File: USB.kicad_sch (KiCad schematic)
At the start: 34 parts, among them J1 USB_C_Receptable_USB2.0, U1 AP2141WG-7, U2 3V3

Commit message: Apply suggestions from Petr Dvorak
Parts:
- added C42: 100n, Capacitor_SMD:C_0402_1005Metric_Pad0.74x0.62mm_HandSolder, symbol Device:C
- added C43: 10u, Capacitor_SMD:C_0805_2012Metric, symbol Device:C
- C1, C2: Comment 50V 100nF X7R ±10% 0402 Multilayer Ceramic Capacitors MLCC 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 -> 50V 100nF X7R ±10% 0402
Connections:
- net GND: now also C42.1, C43.2
- net at D1.1 (A1), F1.2, U1.5 (IN): now also C42.2, C43.1
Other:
- moved on the sheet: C1, C10, C11, C12, C13, C14, C15, C16, C17, C2, D1, D2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

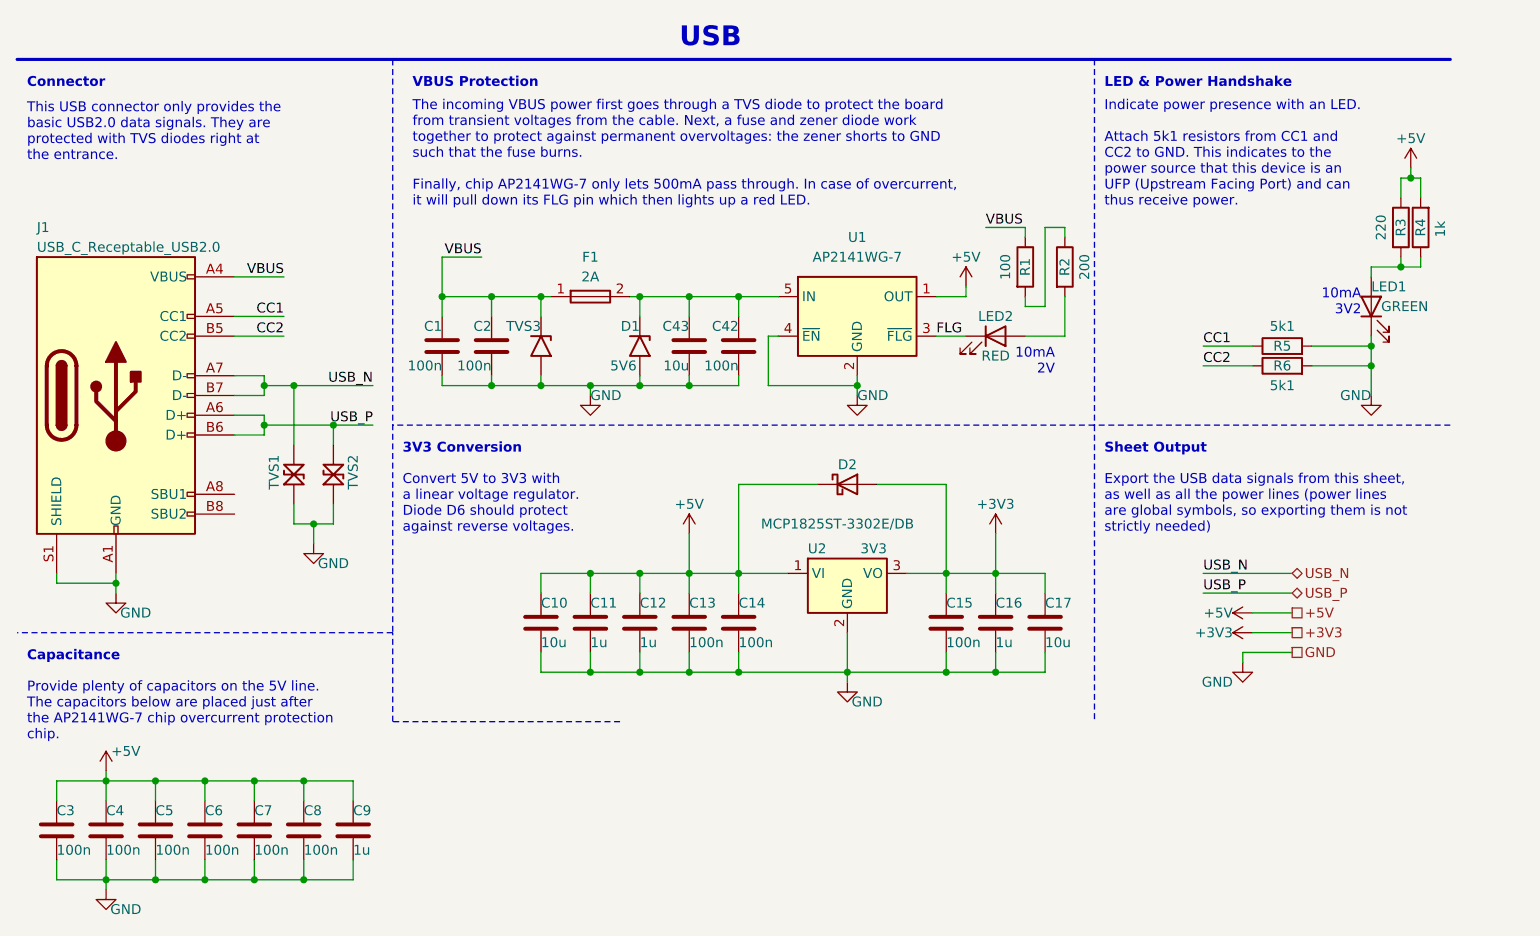
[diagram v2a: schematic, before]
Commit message: Rename capacitors
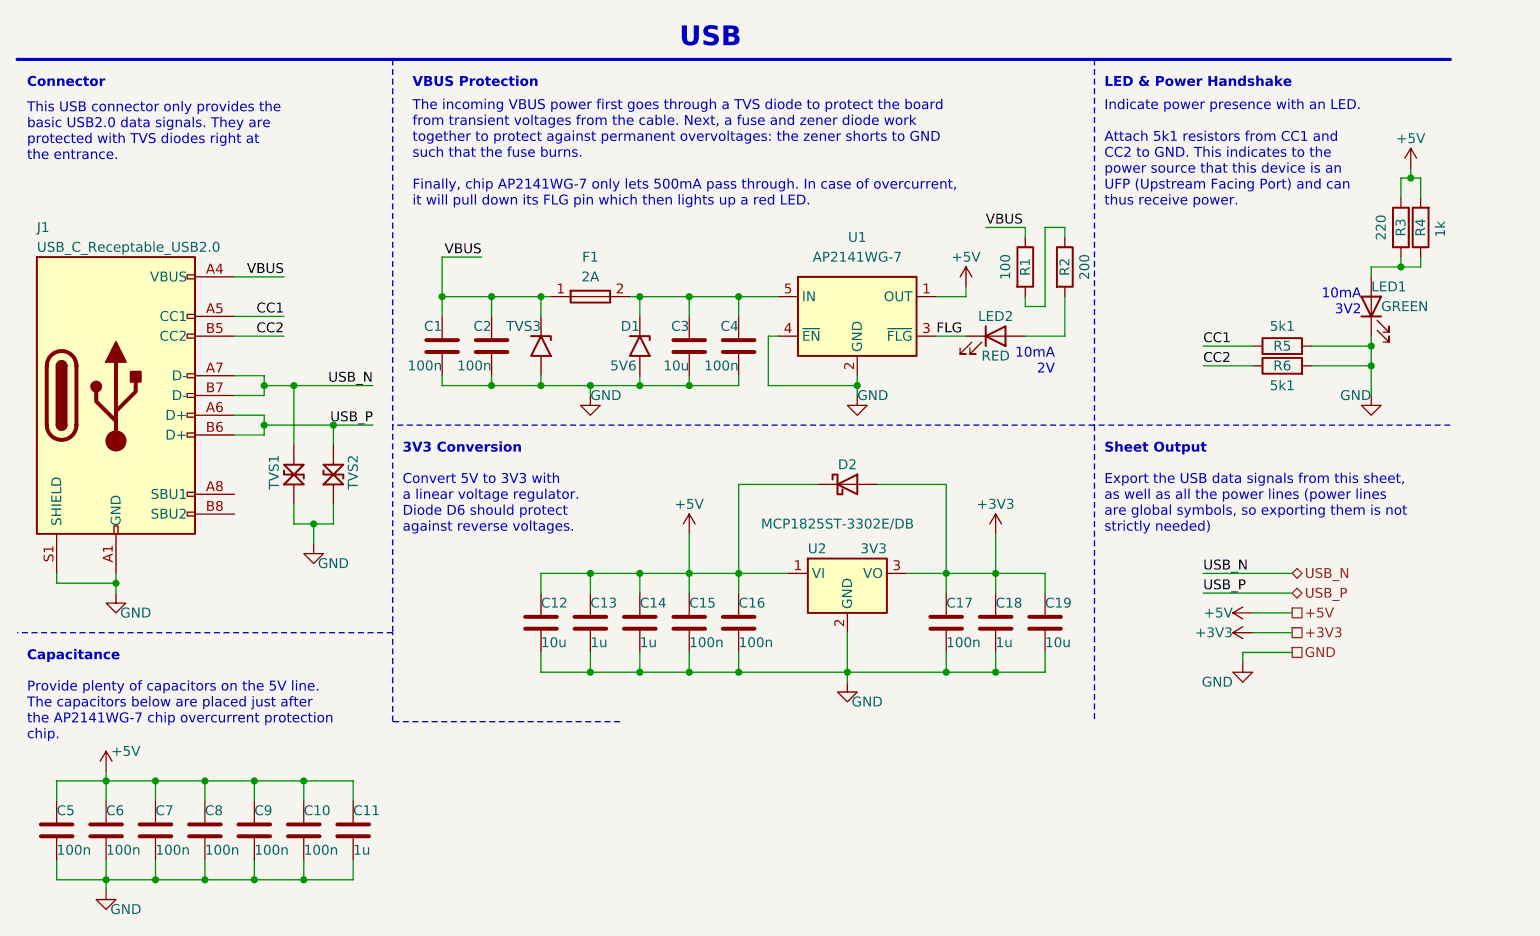
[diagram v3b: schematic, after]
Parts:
- C10: renamed from C8; Comment (none) -> 16V 100nF X7R ±10% 0402
- C11: renamed from C9; Comment (none) -> 25V 1uF X5R ±10% 0402
- C12: renamed from C10; Comment (none) -> 6.3V 10uF X5R ±20% 0402
- C13: renamed from C11; Comment (none) -> 25V 1uF X5R ±10% 0402
- C14: renamed from C12; Comment (none) -> 25V 1uF X5R ±10% 0402
- C15: renamed from C13; Comment (none) -> 16V 100nF X7R ±10% 0402
- C16: renamed from C14; Comment (none) -> 16V 100nF X7R ±10% 0402
- C17: renamed from C15; Comment (none) -> 16V 100nF X7R ±10% 0402
- C18: renamed from C16; Comment (none) -> 25V 1uF X5R ±10% 0402
- C19: renamed from C17; Comment (none) -> 6.3V 10uF X5R ±20% 0402
- C5: renamed from C3; Comment (none) -> 16V 100nF X7R ±10% 0402
- C6: renamed from C4; Comment (none) -> 16V 100nF X7R ±10% 0402
- C7: renamed from C5; Comment (none) -> 16V 100nF X7R ±10% 0402
- C8: renamed from C6; Comment (none) -> 16V 100nF X7R ±10% 0402
- C9: renamed from C7; Comment (none) -> 16V 100nF X7R ±10% 0402
- renumbered C43 to C3, C42 to C4

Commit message: Add production files
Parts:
- TVS3: SPN SMAJ5.0ALFTR-ND -> (none); Supplier DigiKey -> (none)
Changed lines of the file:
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@@
-      (effects (font (size 1.27 1.27)) hide)
-    )
-    (property "Supplier" "DigiKey" (at 87.63 55.88 0)
-      (effects (font (size 1.27 1.27)) hide)
-    )
-    (property "SPN" "SMAJ5.0ALFTR-ND" (at 90.17 55.88 0)
       (effects (font (size 1.27 1.27)) hide)
     )

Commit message: Work on BOM
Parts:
- LED1: JLCPCB Part # (none) -> C7115899
- LED2: JLCPCB Part # (none) -> C5579175
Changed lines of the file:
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@@
       (effects (font (size 1.27 1.27)) hide)
     )
-    (property "JLCPCB Part #" "" (at 173.99 50.8 0)
+    (property "JLCPCB Part #" "C7115899" (at 173.99 50.8 0)
       (effects (font (size 1.27 1.27)) hide)
     )
@@
       (effects (font (size 1.27 1.27)) hide)
     )
-    (property "JLCPCB Part #" "" (at 138.43 41.91 0)
-      (effects (font (size 1.27 1.27)) hide)
-    )
+    (property "JLCPCB Part #" "C5579175" (at 138.43 41.91 0)
+      (effects (font (size 1.27 1.27)) hide)
+    )

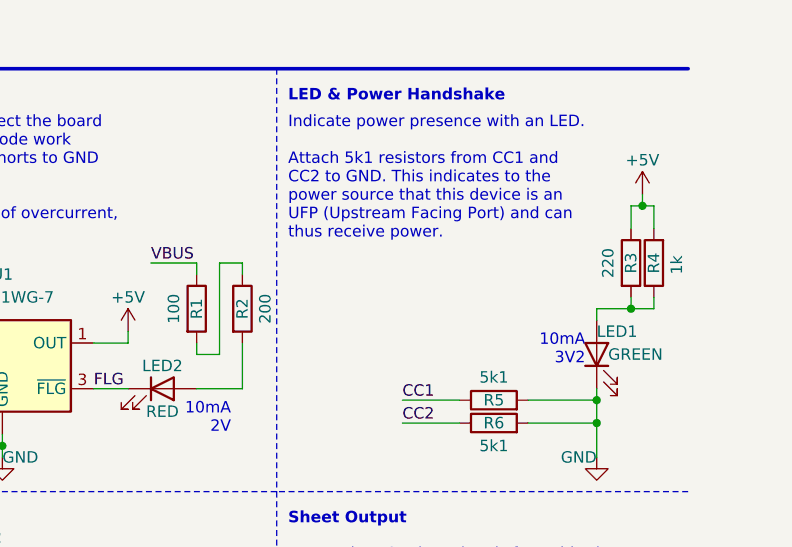
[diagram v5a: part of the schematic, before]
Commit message: Modify resistors for LEDs
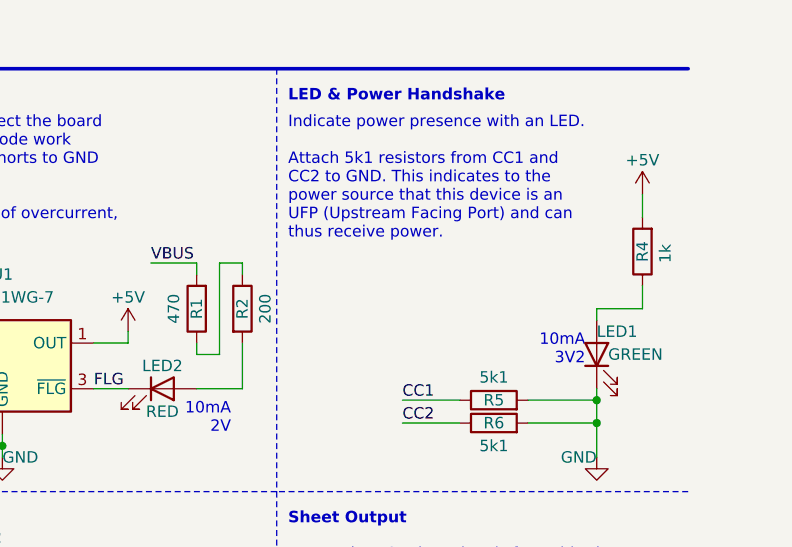
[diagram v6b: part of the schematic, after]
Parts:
- removed R3: 220, Resistor_SMD:R_0402_1005Metric_Pad0.72x0.64mm_HandSolder, symbol Device:R
- R1: value 100 -> 470; JLCPCB Part # C25076 -> C25117; MPN 0402WGF1000TCE -> 0402WGF4700TCE
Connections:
- net VBUS: now also R1.2; no longer R1.1
- net at R2.1: now also R1.1; no longer R1.2
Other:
- moved on the sheet: R4
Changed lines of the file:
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@@
   (junction (at 92.71 49.53) (diameter 0) (color 0 0 0 0)
   )
-  (junction (at 190.5 45.72) (diameter 0) (color 0 0 0 0)
-  )
   (junction (at 36.83 111.76) (diameter 0) (color 0 0 0 0)
   )
@@
   (junction (at 67.31 49.53) (diameter 0) (color 0 0 0 0)
   )
-  (junction (at 191.77 34.29) (diameter 0) (color 0 0 0 0)
-  )
   (junction (at 105.41 97.79) (diameter 0) (color 0 0 0 0)
   )
@@
   )
   (wire (pts (xy 86.36 97.79) (xy 92.71 97.79))
-    (stroke (width 0) (type default))
-  )
-  (wire (pts (xy 193.04 34.29) (xy 191.77 34.29))
     (stroke (width 0) (type default))
   )
@@
     (stroke (width 0) (type default))
   )
-  (wire (pts (xy 193.04 36.83) (xy 193.04 34.29))
+  (wire (pts (xy 191.77 33.02) (xy 191.77 35.56))
     (stroke (width 0) (type default))
   )
@@
     (stroke (width 0) (type default))
   )
-  (wire (pts (xy 193.04 44.45) (xy 193.04 45.72))
+  (wire (pts (xy 191.77 43.18) (xy 191.77 45.72))
     (stroke (width 0) (type default))
   )
@@
   )
   (wire (pts (xy 80.01 97.79) (xy 86.36 97.79))
-    (stroke (width 0) (type default))
-  )
-  (wire (pts (xy 190.5 45.72) (xy 193.04 45.72))
     (stroke (width 0) (type default))
   )
@@
     (stroke (width 0) (type default))
   )
-  (wire (pts (xy 186.69 45.72) (xy 190.5 45.72))
+  (wire (pts (xy 186.69 45.72) (xy 191.77 45.72))
     (stroke (width 0) (type default))
   )
@@
   )
   (wire (pts (xy 24.13 124.46) (xy 24.13 125.73))
-    (stroke (width 0) (type default))
-  )
-  (wire (pts (xy 190.5 44.45) (xy 190.5 45.72))
     (stroke (width 0) (type default))
   )
@@
     (stroke (width 0) (type default))
   )
-  (wire (pts (xy 190.5 34.29) (xy 190.5 36.83))
-    (stroke (width 0) (type default))
-  )
   (wire (pts (xy 67.31 44.45) (xy 67.31 49.53))
     (stroke (width 0) (type default))
@@
     (stroke (width 0) (type dash))
   )
-  (wire (pts (xy 190.5 34.29) (xy 191.77 34.29))
-    (stroke (width 0) (type default))
-  )
   (wire (pts (xy 44.45 59.69) (xy 44.45 60.96))
     (stroke (width 0) (type default))
@@
   )
   (wire (pts (xy 99.06 80.01) (xy 99.06 85.09))
-    (stroke (width 0) (type default))
-  )
-  (wire (pts (xy 191.77 34.29) (xy 191.77 33.02))
     (stroke (width 0) (type default))
   )
@@
     )
   )
-  (symbol (lib_id "Device:R") (at 193.04 40.64 180) (unit 1)
-    (in_bom yes) (on_board yes) (dnp no)
-    (property "Reference" "R4" (at 193.04 40.64 90)
+  (symbol (lib_id "Device:R") (at 191.77 39.37 180) (unit 1)
+    (in_bom yes) (on_board yes) (dnp no)
+    (property "Reference" "R4" (at 191.77 39.37 90)
       (effects (font (size 1.27 1.27)))
     )
-    (property "Value" "1k" (at 195.58 41.91 90)
+    (property "Value" "1k" (at 194.31 40.64 90)
       (effects (font (size 1.27 1.27)) (justify right))
     )
-    (property "Footprint" "Resistor_SMD:R_0402_1005Metric_Pad0.72x0.64mm_HandSolder" (at 194.818 40.64 90)
-      (effects (font (size 1.27 1.27)) hide)
-    )
-    (property "Datasheet" "~" (at 193.04 40.64 0)
-      (effects (font (size 1.27 1.27)) hide)
-    )
-    (property "Manufacturer" "UNI-ROYAL(Uniroyal Elec)" (at 193.04 40.64 0)
-      (effects (font (size 1.27 1.27)) hide)
-    )
-    (property "MPN" "0402WGF1001TCE" (at 193.04 40.64 90)
-      (effects (font (size 1.27 1.27)) hide)
-    )
-    (property "JLCPCB Part #" "C11702" (at 193.04 40.64 90)
+    (property "Footprint" "Resistor_SMD:R_0402_1005Metric_Pad0.72x0.64mm_HandSolder" (at 193.548 39.37 90)
+      (effects (font (size 1.27 1.27)) hide)
+    )
+    (property "Datasheet" "~" (at 191.77 39.37 0)
+      (effects (font (size 1.27 1.27)) hide)
+    )
+    (property "Manufacturer" "UNI-ROYAL(Uniroyal Elec)" (at 191.77 39.37 0)
+      (effects (font (size 1.27 1.27)) hide)
+    )
+    (property "MPN" "0402WGF1001TCE" (at 191.77 39.37 90)
+      (effects (font (size 1.27 1.27)) hide)
+    )
+    (property "JLCPCB Part #" "C11702" (at 191.77 39.37 90)
       (effects (font (size 1.27 1.27)) hide)
     )
@@
     )
   )
-  (symbol (lib_id "Device:R") (at 142.24 45.72 0) (unit 1)
+  (symbol (lib_id "Device:R") (at 142.24 45.72 180) (unit 1)
     (in_bom yes) (on_board yes) (dnp no)
     (property "Reference" "R1" (at 142.24 45.72 90)
       (effects (font (size 1.27 1.27)))
     )
-    (property "Value" "100" (at 139.7 45.72 90)
+    (property "Value" "470" (at 139.7 45.72 90)
       (effects (font (size 1.27 1.27)))
     )
-    (property "Footprint" "Resistor_SMD:R_0402_1005Metric_Pad0.72x0.64mm_HandSolder" (at 140.462 45.72 90)
+    (property "Footprint" "Resistor_SMD:R_0402_1005Metric_Pad0.72x0.64mm_HandSolder" (at 144.018 45.72 90)
       (effects (font (size 1.27 1.27)) hide)
     )
@@
       (effects (font (size 1.27 1.27)) hide)
     )
-    (property "Manufacturer" "UNI-ROYAL(Uniroyal Elec)" (at 142.24 45.72 90)
-      (effects (font (size 1.27 1.27)) hide)
-    )
-    (property "MPN" "0402WGF1000TCE" (at 142.24 45.72 90)
-      (effects (font (size 1.27 1.27)) hide)
-    )
-    (property "JLCPCB Part #" "C25076" (at 142.24 45.72 90)
+    (property "Manufacturer" "UNI-ROYAL(Uniroyal Elec)" (at 142.24 45.72 0)
+      (effects (font (size 1.27 1.27)) hide)
+    )
+    (property "MPN" "0402WGF4700TCE" (at 142.24 45.72 90)
+      (effects (font (size 1.27 1.27)) hide)
+    )
+    (property "JLCPCB Part #" "C25117" (at 142.24 45.72 90)
       (effects (font (size 1.27 1.27)) hide)
     )
@@
         )
       )
-    )
-  )
-  (symbol (lib_id "Device:R") (at 190.5 40.64 0) (unit 1)
-    (in_bom yes) (on_board yes) (dnp no)
-    (property "Reference" "R3" (at 190.5 40.64 90)
-      (effects (font (size 1.27 1.27)))
-    )
-    (property "Value" "220" (at 187.96 40.64 90)
-      (effects (font (size 1.27 1.27)))
-    )
-    (property "Footprint" "Resistor_SMD:R_0402_1005Metric_Pad0.72x0.64mm_HandSolder" (at 188.722 40.64 90)
-      (effects (font (size 1.27 1.27)) hide)
-    )
-    (property "Datasheet" "~" (at 190.5 40.64 0)
-      (effects (font (size 1.27 1.27)) hide)
-    )
-    (property "Manufacturer" "UNI-ROYAL(Uniroyal Elec)" (at 190.5 40.64 90)
-      (effects (font (size 1.27 1.27)) hide)
-    )
-    (property "MPN" "0402WGF2200TCE" (at 190.5 40.64 90)
-      (effects (font (size 1.27 1.27)) hide)
-    )
-    (property "JLCPCB Part #" "C25091" (at 190.5 40.64 90)
-      (effects (font (size 1.27 1.27)) hide)
-    )
-    (pin "2")
-    (pin "1")
-    (instances
-      (project "tiny-scarab"
-        (path "/156c5422-ee07-49a4-8263-a2dbd26b90bd/99c48f54-1f97-4ff9-8db4-28f0cf987802"
-          (reference "R3") (unit 1)
-        )
-      )

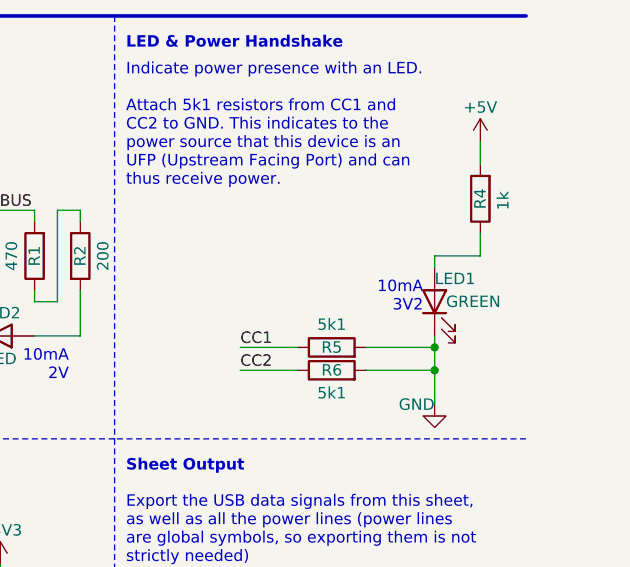
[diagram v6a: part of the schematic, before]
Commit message: Rename 'modify_designators.py' into 'kicad_designators.py'
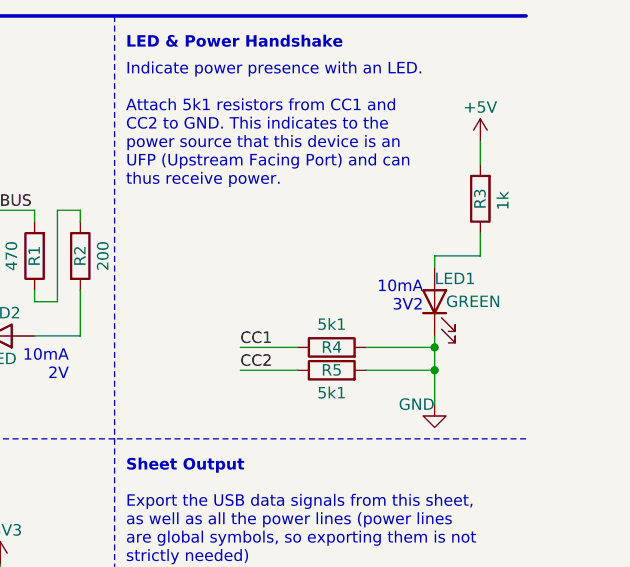
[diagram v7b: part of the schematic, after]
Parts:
- renumbered R4 to R3, R5 to R4, R6 to R5
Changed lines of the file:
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@@
   (symbol (lib_id "Device:R") (at 191.77 39.37 180) (unit 1)
     (in_bom yes) (on_board yes) (dnp no)
-    (property "Reference" "R4" (at 191.77 39.37 90)
+    (property "Reference" "R3" (at 191.77 39.37 90)
       (effects (font (size 1.27 1.27)))
     )
@@
       (project "tiny-scarab"
         (path "/156c5422-ee07-49a4-8263-a2dbd26b90bd/99c48f54-1f97-4ff9-8db4-28f0cf987802"
-          (reference "R4") (unit 1)
+          (reference "R3") (unit 1)
         )
       )
@@
   (symbol (lib_id "Device:R") (at 175.26 58.42 90) (unit 1)
     (in_bom yes) (on_board yes) (dnp no)
-    (property "Reference" "R6" (at 175.26 58.42 90)
+    (property "Reference" "R5" (at 175.26 58.42 90)
       (effects (font (size 1.27 1.27)))
     )
@@
       (project "tiny-scarab"
         (path "/156c5422-ee07-49a4-8263-a2dbd26b90bd/99c48f54-1f97-4ff9-8db4-28f0cf987802"
-          (reference "R6") (unit 1)
+          (reference "R5") (unit 1)
         )
       )
@@
   (symbol (lib_id "Device:R") (at 175.26 55.88 90) (unit 1)
     (in_bom yes) (on_board yes) (dnp no)
-    (property "Reference" "R5" (at 175.26 55.88 90)
+    (property "Reference" "R4" (at 175.26 55.88 90)
       (effects (font (size 1.27 1.27)))
     )
@@
       (project "tiny-scarab"
         (path "/156c5422-ee07-49a4-8263-a2dbd26b90bd/99c48f54-1f97-4ff9-8db4-28f0cf987802"
-          (reference "R5") (unit 1)
-        )
-      )
+          (reference "R4") (unit 1)
+        )
+      )
